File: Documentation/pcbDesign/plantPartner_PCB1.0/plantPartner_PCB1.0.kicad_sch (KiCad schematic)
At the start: 37 parts, among them IC1 MPM3610, J1 Conn_01x04, J2 Conn_01x04, J3 Conn_01x04, J4 Screw_Terminal, J5 Screw_Terminal, J6 Screw_Terminal, J7 Conn_01x03, K1 SRD-05VDC-SL-C, Q1 PNP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

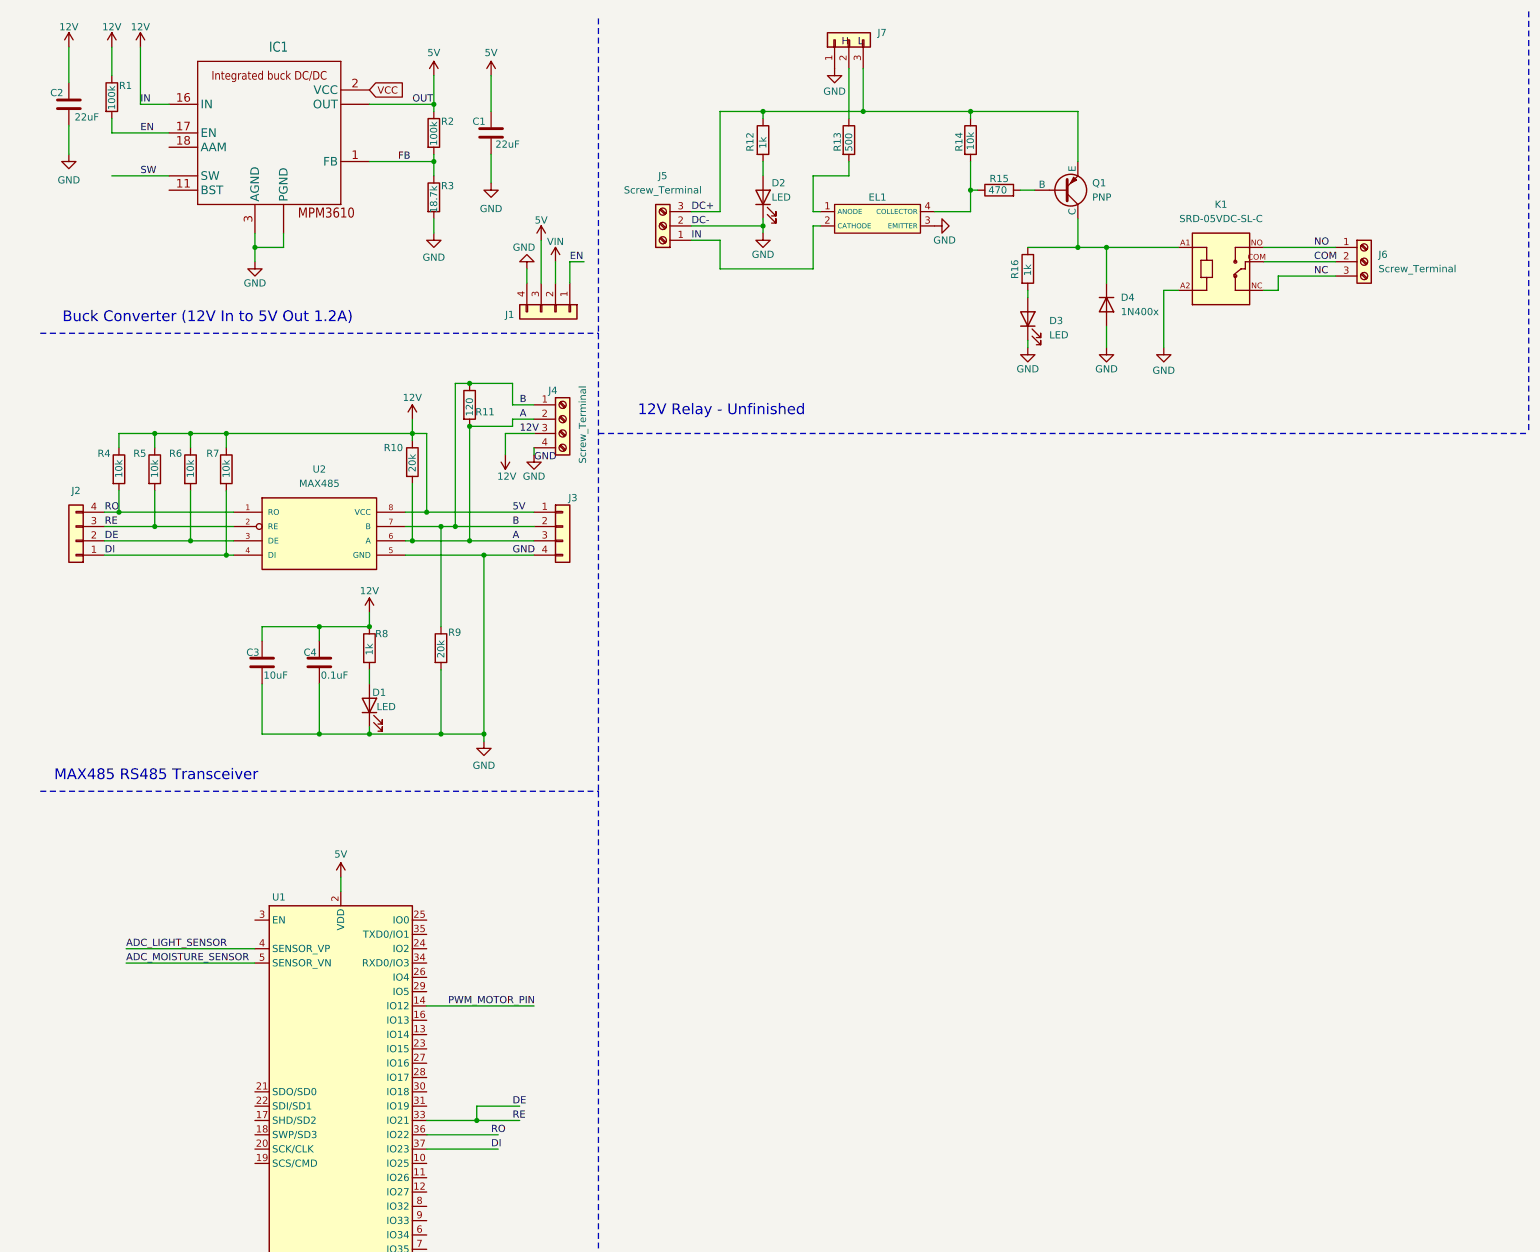
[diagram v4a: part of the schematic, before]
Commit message: Verified the Schematic designs for the RS-485 Transceiver and Buck Converter. I will verify the 5V Relay next and then start routing the PCB itself ASAP
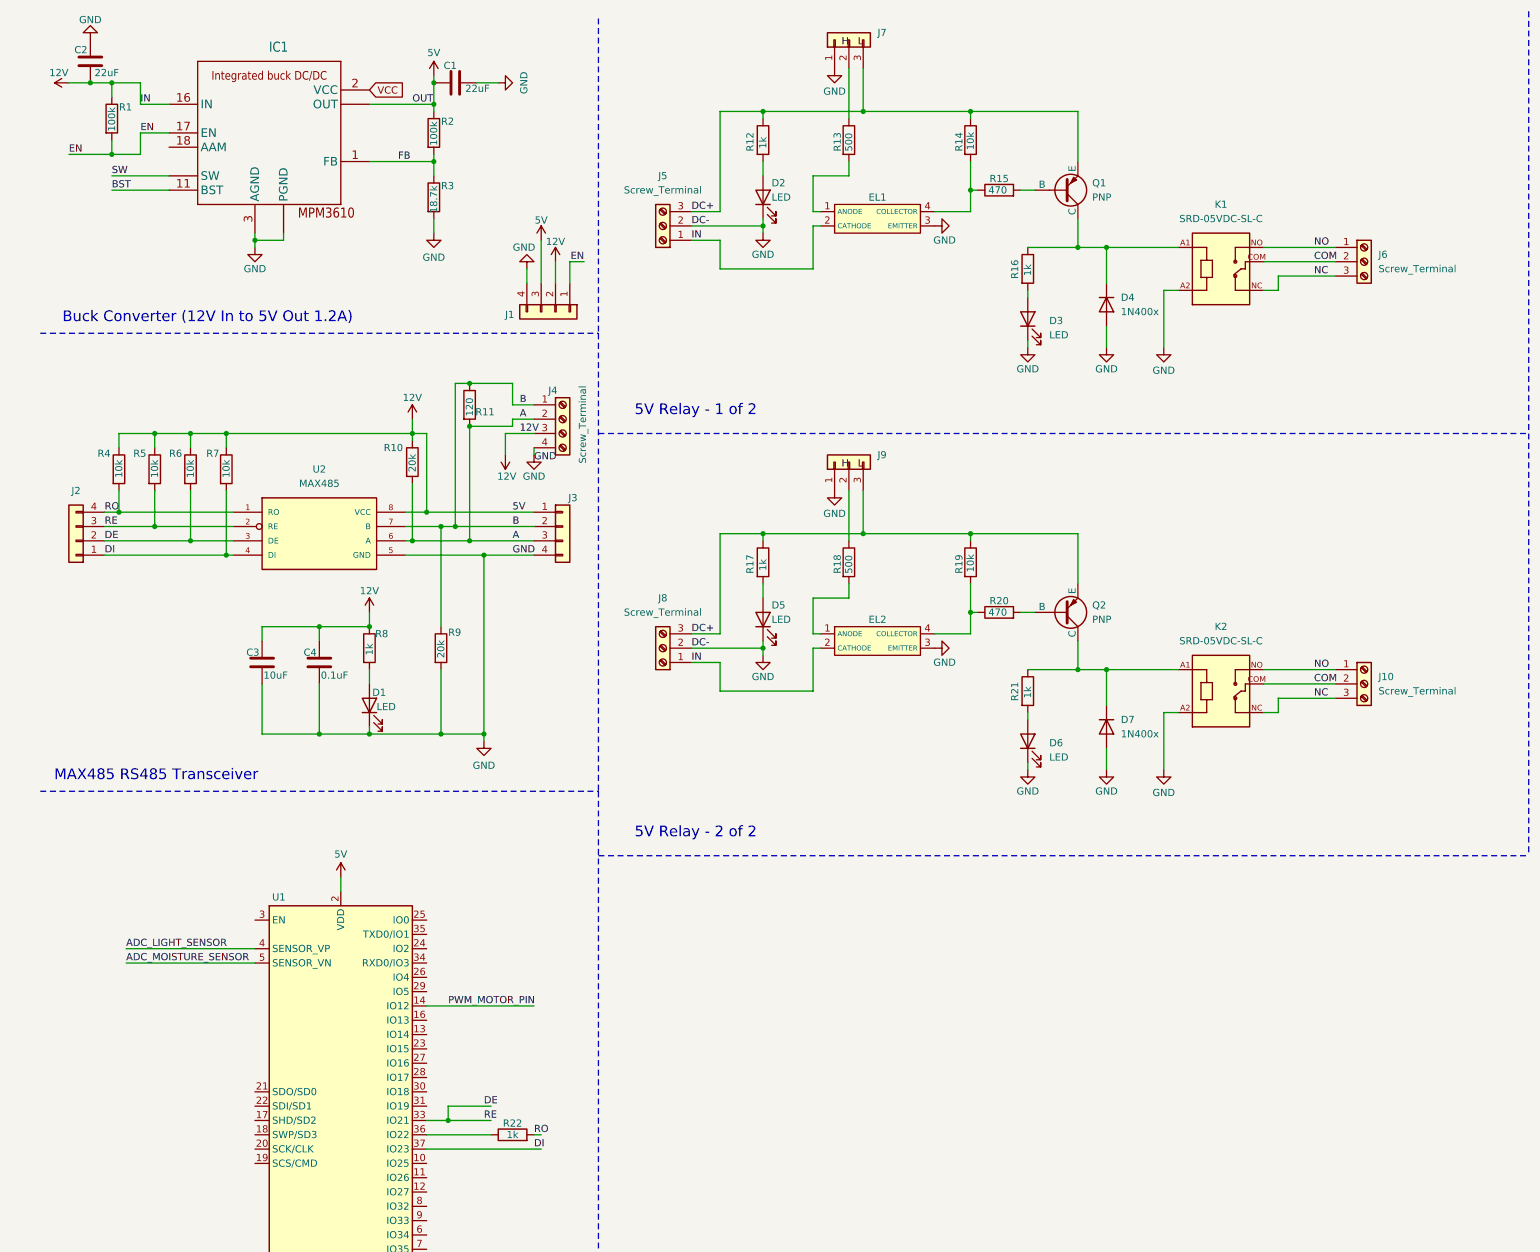
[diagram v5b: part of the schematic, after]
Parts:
- added D5, D6: LED, LED_SMD:LED_0201_0603Metric, symbol Device:LED
- added D7: 1N400x, Diode_THT:D_A-405_P7.62mm_Horizontal, symbol Device:D
- added EL2: ~, MyCustomFootprints:OPTO_EL357N-G, symbol 12V_Relay:EL354(TA)
- added J10, J8: Screw_Terminal, TerminalBlock_Phoenix:TerminalBlock_Phoenix_MKDS-1,5-3-5.08_1x03_P5.08mm_Horizontal, symbol Connector:Screw_Terminal_01x03
- added J9: Conn_01x03, Connector_PinHeader_2.54mm:PinHeader_1x03_P2.54mm_Vertical, symbol Connector_Generic:Conn_01x03
- added K2: SRD-05VDC-SL-C, MyCustomFootprints:RELAY_SRD-05VDC-SL-C, symbol SRD-05VDC-SL-C:SRD-05VDC-SL-C
- added Q2: PNP, Package_TO_SOT_THT:TO-92, symbol Simulation_SPICE:PNP
- added R17, R21: 1k, Resistor_SMD:R_0201_0603Metric, symbol Device:R
- added R18: 500, Resistor_SMD:R_0201_0603Metric, symbol Device:R
- added R19: 10k, Resistor_SMD:R_0201_0603Metric, symbol Device:R
- added R20: 470, Resistor_SMD:R_0201_0603Metric, symbol Device:R
- added R22: 1k, symbol Device:R
- J7: footprint (none) -> Connector_PinHeader_2.54mm:PinHeader_1x03_P2.54mm_Vertical
- K1: footprint SRD-05VDC-SL-C:RELAY_SRD-05VDC-SL-C -> MyCustomFootprints:RELAY_SRD-05VDC-SL-C
- Q1: footprint (none) -> Package_TO_SOT_THT:TO-92
- R16: footprint (none) -> Resistor_SMD:R_0201_0603Metric
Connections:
- net VIN is gone; now on net 12V: J1.2 (Pin_2)
- net 12V: now also EL2.2 (CATHODE), J8.1 (Pin_1)
- net COM: now also J10.2 (Pin_2), K2.COM
- net DC+: now also J8.3 (Pin_3), J9.3 (Pin_3), Q2.3 (E), R17.1, R19.1
- net GND: now also D5.1 (K), D6.1 (K), D7.2 (A), EL2.3 (EMITTER), J8.2 (Pin_2), J9.1 (Pin_1), K2.A2
- net NC: now also J10.3 (Pin_3), K2.NC
- net NO: now also J10.1 (Pin_1), K2.NO
- net RO: now also R22.2; no longer U1.36 (IO22)
- net BST: now reaches IC1.11 (BST)
- new net: D7.1 (K), K2.A1, Q2.1 (C), R21.1
- new net: Q2.2 (B), R20.2
- new net: D6.2 (A), R21.2
- new net: R22.1, U1.36 (IO22)
- new net: EL2.4 (COLLECTOR), R19.2, R20.1
- new net: D5.2 (A), R17.2
- new net: J9.2 (Pin_2), R18.1
- new net: EL2.1 (ANODE), R18.2
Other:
- note added: "5V Relay - 1 of 2"
- note added: "5V Relay - 2 of 2"
- note removed: "12V Relay - Unfinished"
- moved on the sheet: C1, C2, R1

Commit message: Added hours from meeting today and winter break
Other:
- note added: "Double Check resistor and capacitor values since Schematic is 12V not 5V"
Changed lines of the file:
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@@
+		)
+	)
+	(text "Double Check resistor and capacitor values since Schematic is 12V not 5V\n"
+		(exclude_from_sim no)
+		(at 197.104 81.534 0)
+		(effects
+			(font
+				(size 1.27 1.27)
+			)
 		)
 	)

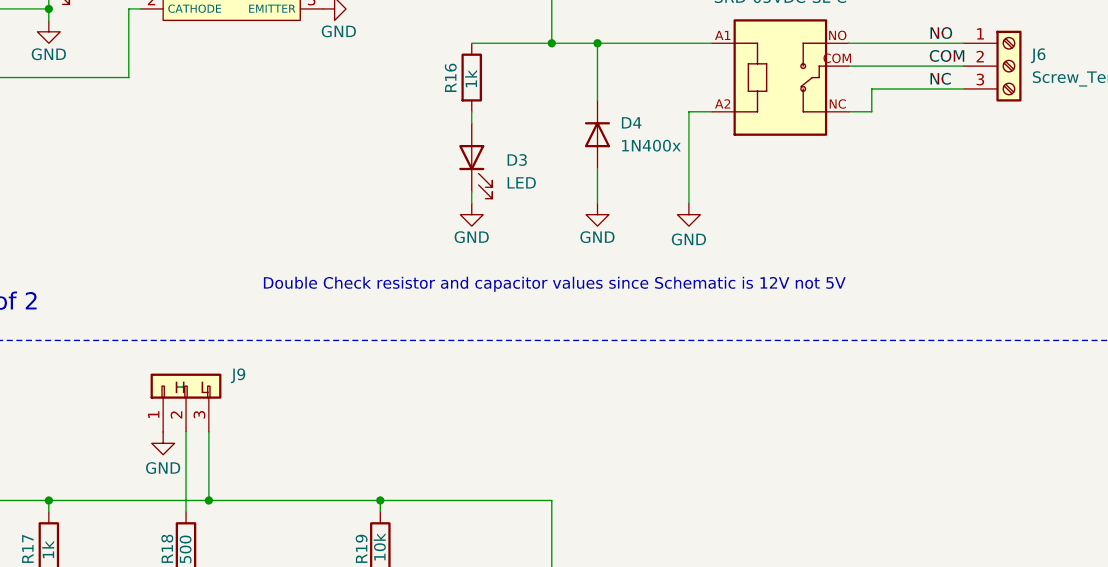
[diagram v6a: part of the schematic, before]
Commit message: Since I was able to copy the Buck Converter and RS-485 Relay verbatim from an online source, verifying them was rather quick but for this 5V relay I am trying to properly simulate and probe its voltage values. I started with KiCad's sim and that was bad so then I moved into LTspice and asked ChatGPT to help convert some of the components to standard SPICE parts since I only took Circuits 1. I am making progress but it's not feeling like it lol
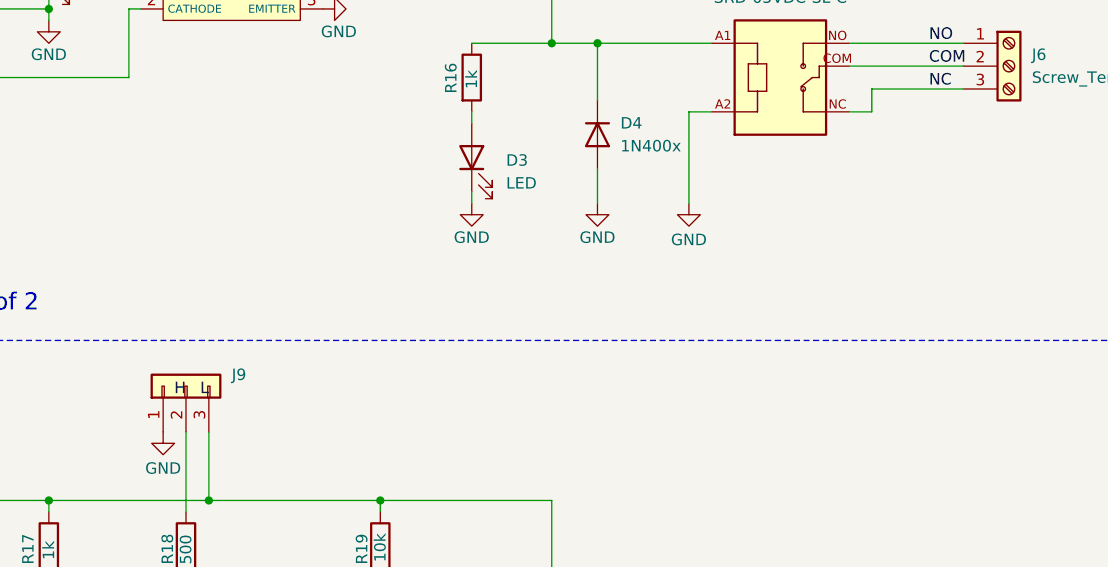
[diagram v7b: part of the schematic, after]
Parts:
- R22: footprint (none) -> Resistor_SMD:R_0201_0603Metric
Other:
- note removed: "Double Check resistor and capacitor values since Schematic is 12V not 5V"
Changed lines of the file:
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@@
 		)
 	)
-	(text "Double Check resistor and capacitor values since Schematic is 12V not 5V\n"
-		(exclude_from_sim no)
-		(at 197.104 81.534 0)
-		(effects
-			(font
-				(size 1.27 1.27)
-			)
-		)
-	)
 	(junction
 		(at 50.8 53.34)
@@
 			)
 		)
-		(property "Footprint" ""
+		(property "Footprint" "Resistor_SMD:R_0201_0603Metric"
 			(at 96.52 213.868 90)
 			(effects

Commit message: Verified circuit. Time to finalize Schematic with symbols that have compatible footprints. Need to add remaining 3D models, testing pins for PCB, and verify relay octocoupler footprint + symbol
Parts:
- added U3: ESP32-DEVKIT-V1, ESP32-DEVKIT-V1:MODULE_ESP32_DEVKIT_V1, symbol ESP32-DEVKIT-V1:ESP32-DEVKIT-V1
- IC1: footprint MyCustomFootprints:CONV_MPM3610GQV-P -> MyCustomFootprints:MPM3610
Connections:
- net GND: now also U3.2 (GND), U3.29 (GND)
- net AAM: now reaches IC1.18 (AAM)
- net PWM_FERTIL_PIN: now reaches U1.16 (IO13)
- net PWM_MOTOR_PIN renamed PWM_WATER_PIN
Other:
- note added: "Add in OPTO_EL357N-G's (EL1 & EL2) footprint, symbol, and 3d model from SnapMagic."
- note added: "Verify that the imported OPTO_EL357N-G is equal to the EL354 that I have been assuming. Import all the 3D models accordingly after, add testing pins on Schematic, route PCB and add any necessary text to it"
- moved on the sheet: C1, C2, IC1, R1, R2, R3
